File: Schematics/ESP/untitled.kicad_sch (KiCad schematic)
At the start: 14 parts, among them J11 Bumper 1, J12 Bumper 2, J14 Conn_02x19_Odd_Even, J15 UltraSconic B, J16 Conn_02x19_Odd_Even, J2 IMU, J7 UltraSonic A, J9 ESP

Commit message: fixed bom
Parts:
- J11, J12, J14, J15, J16, J2, J7, J9: digikey link (none) -> https://www.digikey.com/en/products/detail/sullins-connecto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
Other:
- note added: "ESP Connector"
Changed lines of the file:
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@@
     (stroke (width 0) (type default))
+  )
+  (rectangle (start 215.9 33.02) (end 267.97 66.04)
+    (stroke (width 0) (type default))
+    (fill (type none))
   )
   (rectangle (start 25.4 45.72) (end 90.17 97.79)
@@
     (fill (type none))
   )
+  (text "ESP Connector" (at 218.44 35.56 0)
+    (effects (font (size 1.27 1.27)) (justify left bottom))
+  )
   (text "I2C2_SDA" (at 215.9 100.33 0)
     (effects (font (size 1.27 1.27)) (justify left bottom))
@@
     (effects (font (size 1.27 1.27)) (justify right bottom))
   )
-  (text "Bumper Button" (at 151.13 88.9 0)
+  (text "Bumper Button" (at 146.05 88.9 0)
     (effects (font (size 1.27 1.27)) (justify right bottom))
   )
@@
       (effects (font (size 1.27 1.27)) hide)
     )
+    (property "digikey link" "https://www.digikey.com/en/products/detail/sullins-connector-solutions/PPTC021LFBN-RC/810142" (at 54.61 77.47 0)
+      (effects (font (size 1.27 1.27)) hide)
+    )
     (pin "1")
     (pin "2")
@@
       (effects (font (size 1.27 1.27)) hide)
     )
+    (property "digikey link" "https://www.digikey.com/en/products/detail/sullins-connector-solutions/PPTC041LFBN-RC/810144" (at 67.31 116.84 0)
+      (effects (font (size 1.27 1.27)) hide)
+    )
     (pin "1")
     (pin "2")
@@
     )
     (property "Datasheet" "~" (at 242.57 43.18 0)
+      (effects (font (size 1.27 1.27)) hide)
+    )
+    (property "digikey link" "https://www.digikey.com/en/products/detail/sullins-connector-solutions/PPPC042LFBN-RC/810244" (at 242.57 43.18 0)
       (effects (font (size 1.27 1.27)) hide)
     )
@@
     )
     (property "Datasheet" "~" (at 154.94 105.41 0)
+      (effects (font (size 1.27 1.27)) hide)
+    )
+    (property "digikey link" "https://www.digikey.com/en/products/detail/sullins-connector-solutions/PPPC192LFBN-RC/810258?s=N4IgTCBcDaIAoIMIEYCcYAyAxAQgOQFoAlREAXQF8g DigiKey" (at 154.94 105.41 0)
       (effects (font (size 1.27 1.27)) hide)
     )
@@
       (effects (font (size 1.27 1.27)) hide)
     )
+    (property "digikey link" "https://www.digikey.com/en/products/detail/sullins-connector-solutions/PPTC041LFBN-RC/810144" (at 62.23 142.24 0)
+      (effects (font (size 1.27 1.27)) hide)
+    )
     (pin "1")
     (pin "2")
@@
     )
     (property "Datasheet" "~" (at 234.95 115.57 0)
+      (effects (font (size 1.27 1.27)) hide)
+    )
+    (property "digikey link" "https://www.digikey.com/en/products/detail/sullins-connector-solutions/PPPC192LFBN-RC/810258?s=N4IgTCBcDaIAoIMIEYCcYAyAxAQgOQFoAlREAXQF8g DigiKey" (at 234.95 115.57 0)
       (effects (font (size 1.27 1.27)) hide)
     )
@@
       (effects (font (size 1.27 1.27)) hide)
     )
+    (property "digikey link" "https://www.digikey.com/en/products/detail/sullins-connector-solutions/PPPC071LFBN-RC/810179?s=N4IgTCBcDaIAoIMIAYDsBGAMgMQEIDkBaAJUQAIQBdAXyA" (at 187.96 101.6 0)
+      (effects (font (size 1.27 1.27)) hide)
+    )
     (pin "1")
     (pin "2")
@@
       (effects (font (size 1.27 1.27)) hide)
     )
+    (property "digikey link" "https://www.digikey.com/en/products/detail/sullins-connector-solutions/PPTC021LFBN-RC/810142" (at 54.61 60.96 0)
+      (effects (font (size 1.27 1.27)) hide)
+    )

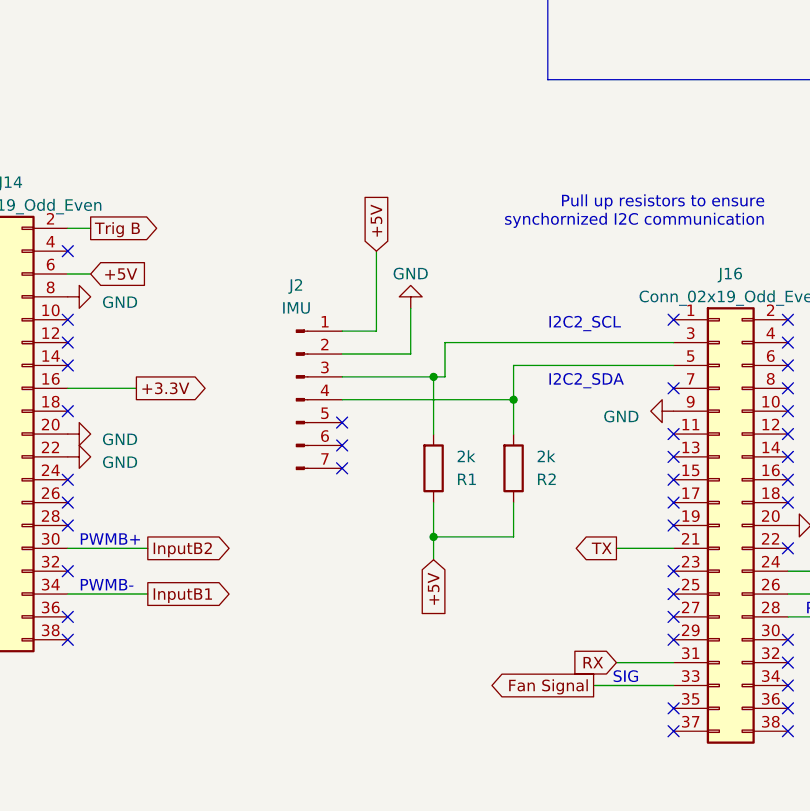
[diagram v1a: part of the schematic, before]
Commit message: fixed 3.3v for IMU
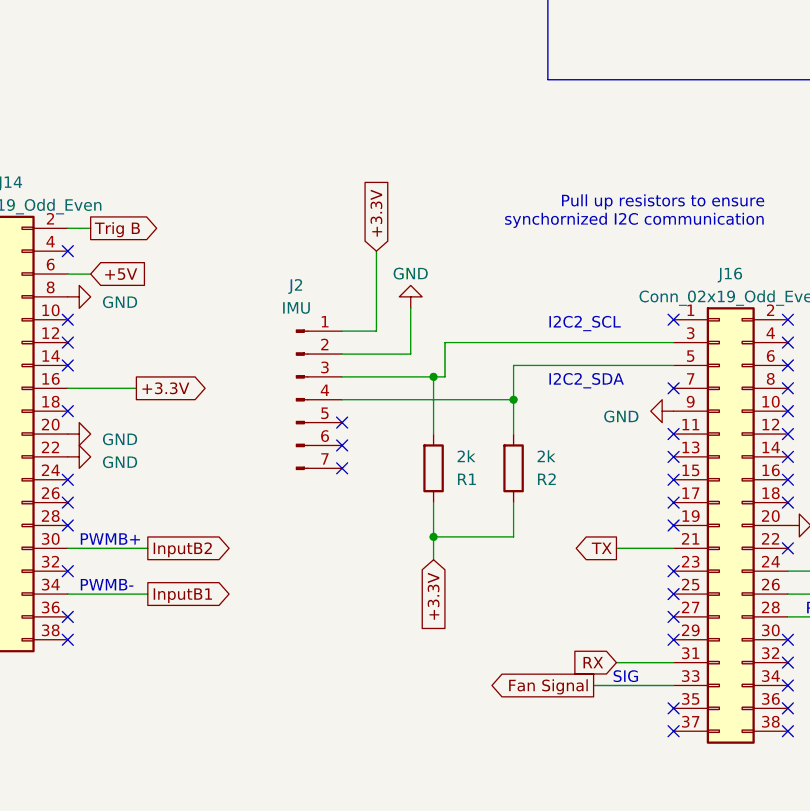
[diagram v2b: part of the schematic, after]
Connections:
- net +3.3V: now also J2.1 (Pin_1), R1.1, R2.1
- net +5V: no longer J2.1 (Pin_1), R1.1, R2.1
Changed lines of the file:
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@@
+    )
+  )
+  (global_label "+3.3V" (shape input) (at 203.2 119.38 270) (fields_autoplaced)
+    (effects (font (size 1.27 1.27)) (justify right))
+    (property "Intersheetrefs" "${INTERSHEET_REFS}" (at 203.2 127.9706 90)
+      (effects (font (size 1.27 1.27)) (justify right) hide)
     )
   )
@@
     )
   )
-  (global_label "+5V" (shape input) (at 203.2 119.38 270) (fields_autoplaced)
-    (effects (font (size 1.27 1.27)) (justify right))
-    (property "Intersheetrefs" "${INTERSHEET_REFS}" (at 203.2 126.1563 90)
-      (effects (font (size 1.27 1.27)) (justify right) hide)
-    )
-  )
   (global_label "Trig B" (shape input) (at 44.45 139.7 180) (fields_autoplaced)
     (effects (font (size 1.27 1.27)) (justify right))
@@
     )
   )
-  (global_label "+5V" (shape input) (at 196.85 85.09 90) (fields_autoplaced)
-    (effects (font (size 1.27 1.27)) (justify left))
-    (property "Intersheetrefs" "${INTERSHEET_REFS}" (at 196.85 78.3137 90)
-      (effects (font (size 1.27 1.27)) (justify right) hide)
-    )
-  )
   (global_label "Trig A" (shape output) (at 143.51 125.73 180) (fields_autoplaced)
     (effects (font (size 1.27 1.27)) (justify right))
@@
     )
   )
+  (global_label "+3.3V" (shape input) (at 196.85 85.09 90) (fields_autoplaced)
+    (effects (font (size 1.27 1.27)) (justify left))
+    (property "Intersheetrefs" "${INTERSHEET_REFS}" (at 196.85 76.4994 90)
+      (effects (font (size 1.27 1.27)) (justify left) hide)
+    )
+  )

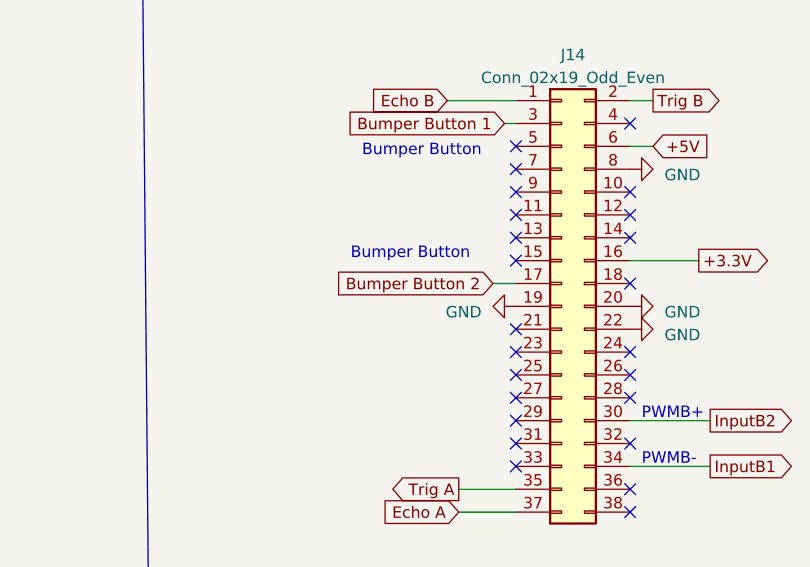
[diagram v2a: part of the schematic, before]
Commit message: Added footprints for battery input and battery charger with BOM updates
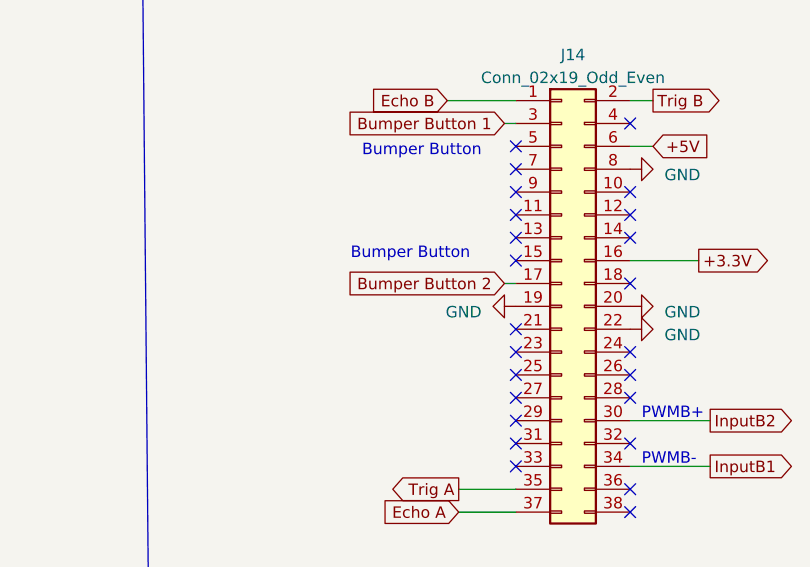
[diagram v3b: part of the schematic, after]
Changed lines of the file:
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@@
     (stroke (width 0) (type default))
   )
-  (wire (pts (xy 147.32 102.87) (xy 149.86 102.87))
+  (wire (pts (xy 148.59 102.87) (xy 149.86 102.87))
     (stroke (width 0) (type default))
   )
@@
     (effects (font (size 1.27 1.27)) (justify left bottom))
   )
-  (global_label "Bumper Button 2" (shape input) (at 147.32 102.87 180) (fields_autoplaced)
+  (global_label "Bumper Button 2" (shape input) (at 148.59 102.87 180) (fields_autoplaced)
     (effects (font (size 1.27 1.27)) (justify right))
-    (property "Intersheetrefs" "${INTERSHEET_REFS}" (at 128.3762 102.87 0)
+    (property "Intersheetrefs" "${INTERSHEET_REFS}" (at 129.6462 102.87 0)
       (effects (font (size 1.27 1.27)) (justify right) hide)
     )
